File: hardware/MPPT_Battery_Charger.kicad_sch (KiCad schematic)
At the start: 78 parts, among them Q24 SI7414DN-T1-E3, Q25 SI7414DN-T1-E3, Q5 SI7414DN-T1-E3, Q6 SI7414DN-T1-E3, Q8 SI2302DDS-T1-GE3, U22 BQ24650RVAT, U26 LMV321RIYLT, U28 LMV321RIYLT, U4 INA199C1DCKR

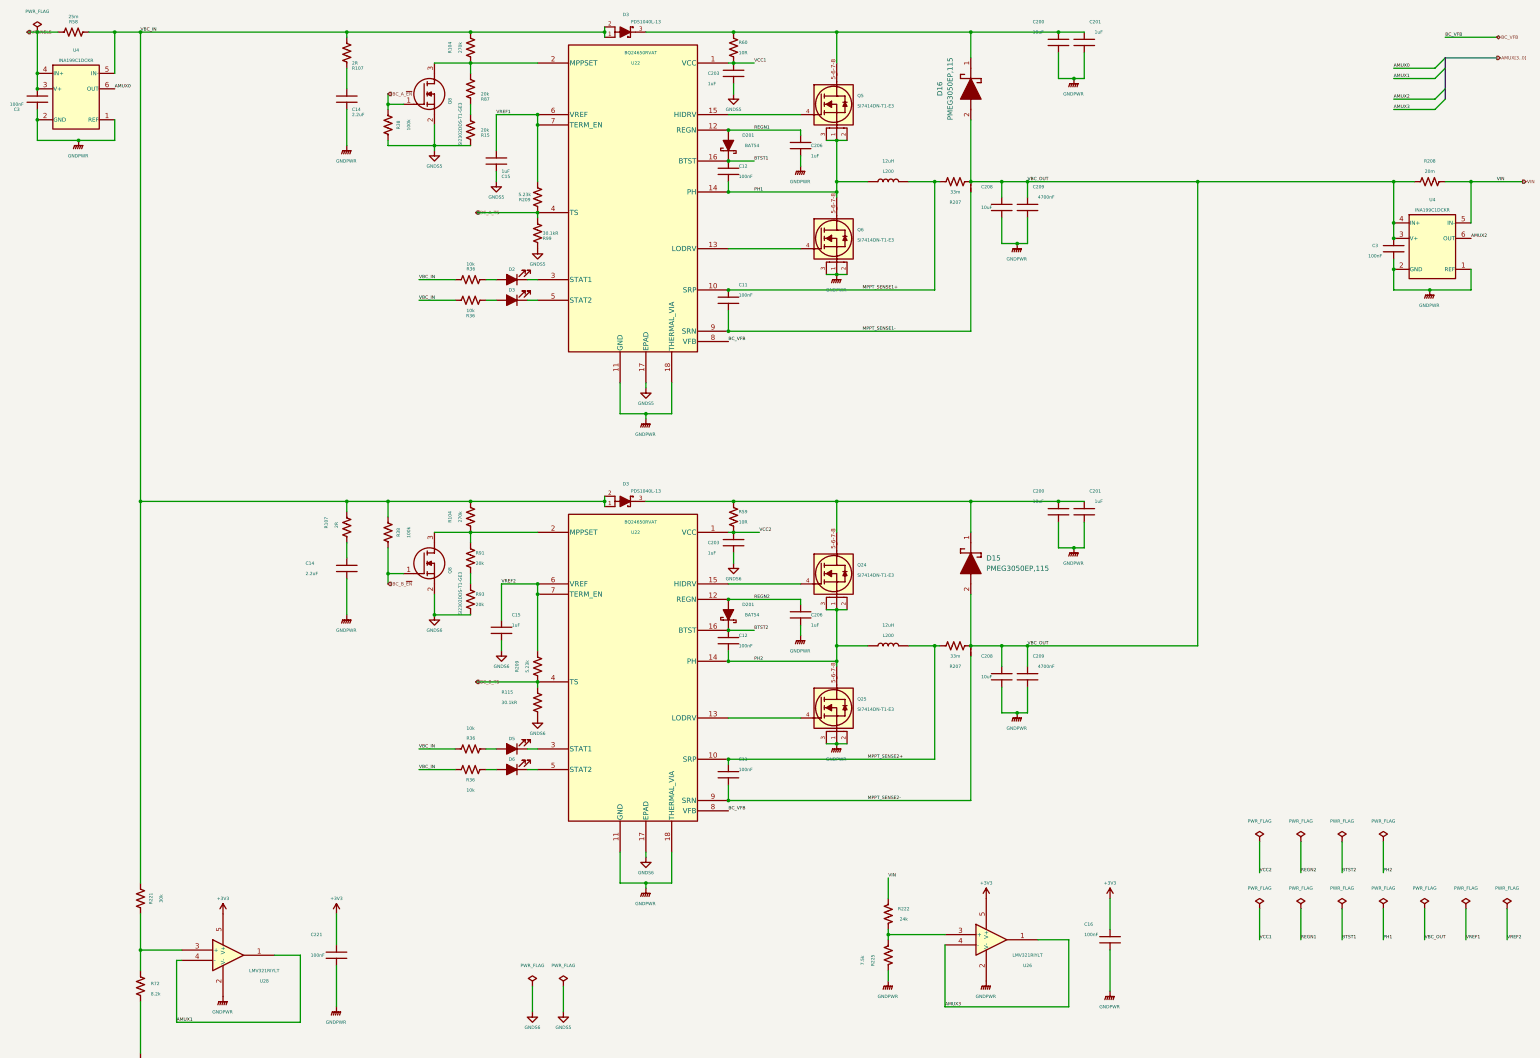
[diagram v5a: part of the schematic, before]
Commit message: hardware: Improving the readability of schematics
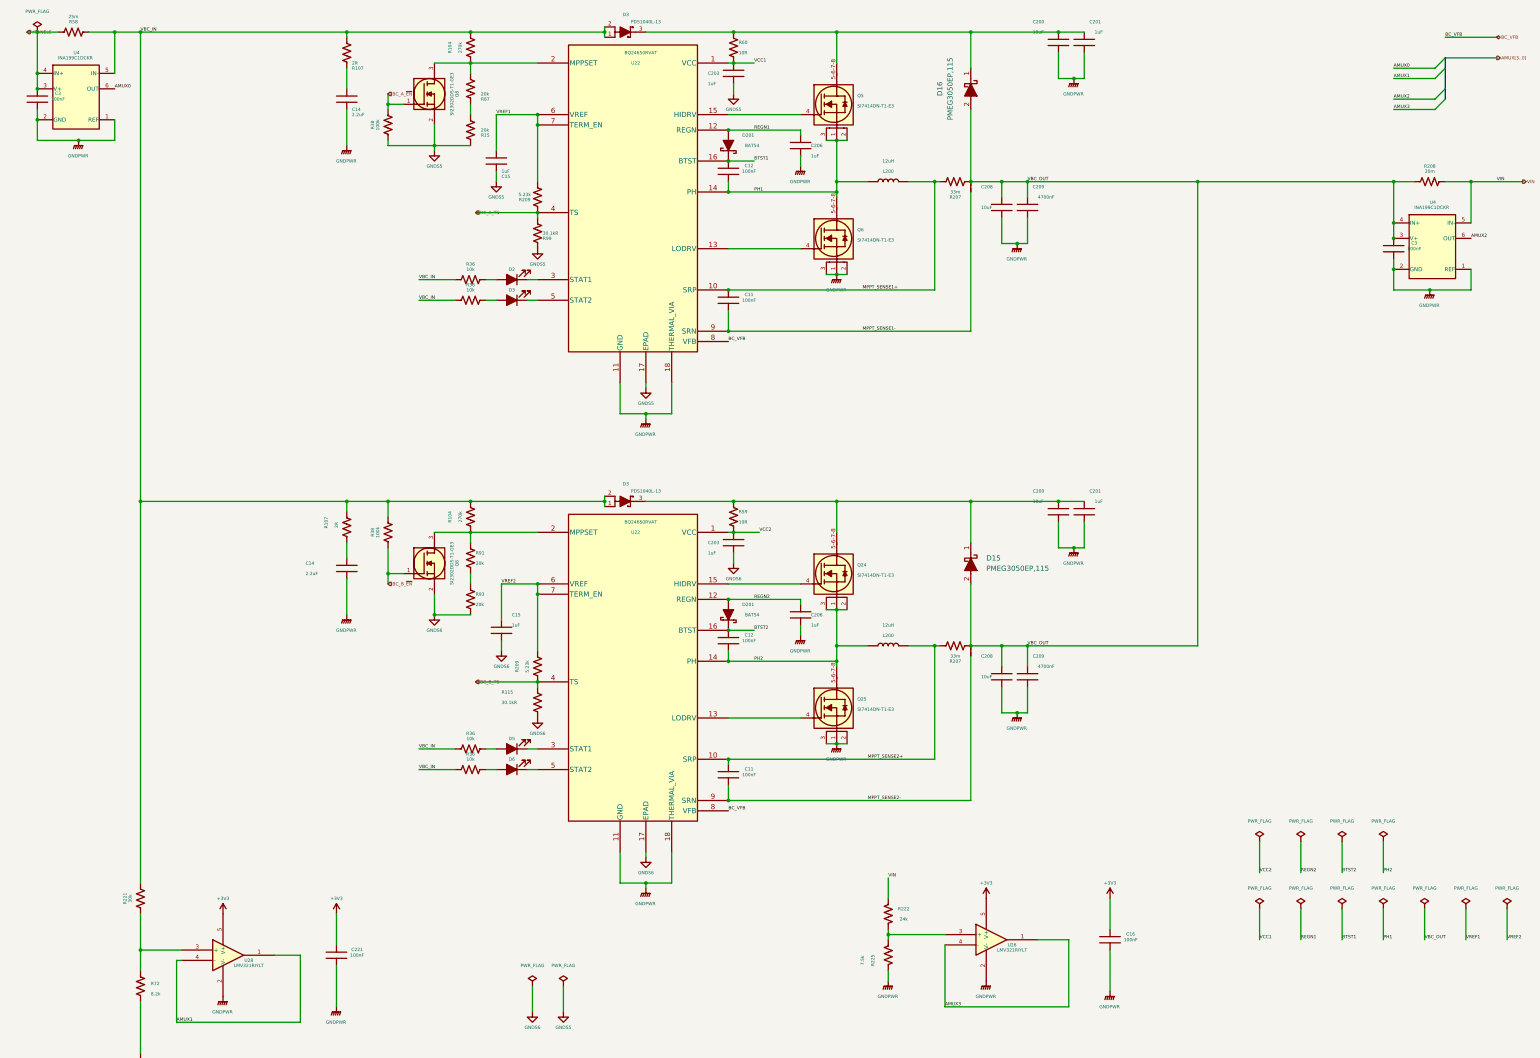
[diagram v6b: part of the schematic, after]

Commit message: hardware: Improving the readability of schematic
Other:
- note added: "ANALOG SIGNALS"
- note added: "POWER FLAGS"
- note added: "TEST POINTS"
- moved on the sheet: C16, R222, R225, U26

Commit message: hardware: Making improvements for first release
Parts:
- C11, C12, C16, C221, C3: MPN (none) -> C0603C104K5RACTU; Manufacturer (none) -> KEMET; Package (none) -> SMD 0603; automotive Yes -> (none); automotive grade Grade 1 -> (none); capacitance 0.10 μF -> (none); category Cap -> (none); device class L1 Passive Components -> (none); device class L2 Capacitors -> (none); device class L3 Ceramic Capacitors -> (none); digikey description CAP CER 0.1UF 50V X7R 0603 -> (none); digikey part number 399-5089-2-ND -> (none); height 0.87mm -> (none); lead free Yes -> (none); library id 73022d3323b2b2b8 -> (none); manufacturer KEMET -> (none); material Ceramic -> (none); mouser part number 80-C0603C104K5R7867 -> (none); package 0603 -> (none); rohs Yes -> (none); temperature characteristic X7R -> (none); temperature coefficient 30ppm/°C -> (none); temperature range high +125°C -> (none); temperature range low -55°C -> (none); tolerance 0.1 -> (none); voltage rating 50 V -> (none)
- C15, C201, C203, C206: MPN (none) -> C0805C105K5RACTU; Manufacturer (none) -> KEMET; Package (none) -> SMD 0805; capacitance 1uF -> (none); category Cap -> (none); device class L1 Passive Components -> (none); device class L2 Capacitors -> (none); device class L3 Ceramic Capacitors -> (none); digikey description CAP CER 1UF 50V X7R 0805 -> (none); digikey part number 399-7409-2-ND -> (none); height 1.4mm -> (none); ipc land pattern name CAPC200125X787 -> (none); lead free yes -> (none); library id ac83af3950e2a3c3 -> (none); manufacturer Kemet -> (none); material Ceramic -> (none); mouser description Multilayer Ceramic Capacitors MLCC - SMD/SMT 1uF 50 Volts 1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 -> (none); mouser part number 80-C0805C105K5R -> (none); package 0805 (2012 metric) -> (none); rohs yes -> (none); standoff height 0mm -> (none); temperature characteristic X7R -> (none); temperature range high +125°C -> (none); temperature range low -55°C -> (none); tolerance 10% -> (none); voltage rating 50V -> (none)
- C200, C208: MPN (none) -> C1210C106K5RACTU; Manufacturer (none) -> KEMET; Package (none) -> SMD 1210; automotive No -> (none); capacitance 10uF -> (none); category Cap -> (none); device class L1 Passive Components -> (none); device class L2 Capacitors -> (none); device class L3 Ceramic Capacitors -> (none); digikey description CAP CER 10UF 50V X7R 1210 -> (none); digikey part number 399-11629-1-ND -> (none); height 2.8mm -> (none); ipc land pattern name CAPC320250X250 -> (none); lead free Yes -> (none); library id 80b9cd679ce51e4b -> (none); manufacturer KEMET -> (none); material Ceramic -> (none); mouser description Multilayer Ceramic Capacitors MLCC - SMD/SMT 50volts 10uF 1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 -> (none); mouser part number 80-C1210C106K5R -> (none); package 1210 -> (none); rohs Yes -> (none); temperature characteristic X7R -> (none); temperature coefficient 15% -> (none); temperature range high +125°C -> (none); temperature range low -55°C -> (none); tolerance 10% -> (none); voltage rating 50V -> (none)
- JP2: value SolderJumper_2_Bridged -> N/A; MPN (none) -> N/A; Manufacturer (none) -> N/A; Package (none) -> N/A
- Q8: Height 1.12 -> (none); MPN (none) -> SI2302DDS-T1-GE3; Manufacturer (none) -> Vishay; Manufacturer_Name Vishay -> (none); Manufacturer_Part_Number SI2302DDS-T1-GE3 -> (none); Mouser Part Number 78-SI2302DDS-T1-GE3 -> (none); Mouser Price/Stock https://www.mouser.co.uk/ProductDetail/Vishay-Semiconductor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 -> (none); Package (none) -> SOT-23-3
- R207: MPN (none) -> WSL2010R0330FEA; Manufacturer (none) -> Vishay; Package (none) -> SMD 2010
- R208: Arrow Part Number WSL2010R0200FEA -> (none); Arrow Price/Stock https://www.arrow.com/en/products/wsl2010r0200fea/vishay -> (none); MPN (none) -> WSL2010R0200FEA; Manufacturer (none) -> Vishay; Manufacturer_Name Vishay -> (none); Manufacturer_Part_Number WSL2010R0200FEA -> (none); Mouser Part Number 71-WSL2010R0200FEA -> (none); Mouser Price/Stock https://www.mouser.co.uk/ProductDetail/Vishay-Dale/WSL2010R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 -> (none); Package (none) -> SMD 2010
- R221: MPN (none) -> CRCW060330K0FKEAHP; Manufacturer (none) -> Vishay; Package (none) -> SMD 0603
- R222: symbol CRCW060324K0FKEAHP:RES -> CRCW060324K0FKEAHP:CRCW060324K0FKEAHP; MPN (none) -> CRCW060324K0FKEAHP; Manufacturer (none) -> Vishay; Package (none) -> SMD 0603
- R225: MPN (none) -> CRCW06037K50FKEAHP; Manufacturer (none) -> Vishay; Package (none) -> SMD 0603; automotive Yes -> (none); automotive grade Grade 0 -> (none); category Res -> (none); composition Thick Film -> (none); device class L1 Passive Components -> (none); device class L2 Resistors -> (none); device class L3 Chip SMD Resistors -> (none); height 0.55mm -> (none); ipc land pattern name RESC16085X45 -> (none); lead free Yes -> (none); library id ac0eb7131481e5d0 -> (none); manufacturer Vishay -> (none); package 0603 -> (none); power 250mW -> (none); power rating 0.33W -> (none); resistance 7.5kΩ -> (none); rohs Yes -> (none); series CRCW-HP e3 -> (none); temperature coefficient 100ppm/°C -> (none); temperature range high +155°C -> (none); temperature range low -55°C -> (none); tolerance 1% -> (none); voltage rating 75V -> (none)
- R38: Arrow Part Number CRCW0603100KFKEAHP -> (none); Arrow Price/Stock https://www.arrow.com/en/products/crcw0603100kfkeahp/vishay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 -> (none); Height 0.55 -> (none); MPN (none) -> CRCW0603100KFKEAHP; Manufacturer (none) -> Vishay; Manufacturer_Name Vishay -> (none); Manufacturer_Part_Number CRCW0603100KFKEAHP -> (none); Mouser Part Number 71-CRCW0603100KFKEAH -> (none); Mouser Price/Stock https://www.mouser.co.uk/ProductDetail/Vishay-Dale/CRCW0603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 -> (none); Package (none) -> SMD 0603
- U22: MPN (none) -> BQ24650RVAT; Manufacturer (none) -> TI; Package (none) -> VQFN-16
- U26, U28: MPN (none) -> LMV321RIYLT; Manufacturer (none) -> STMicroelectronics; Package (none) -> SOT-23-5
- U4: symbol INA199C1DCKR:INA199xxDCK -> INA199C1DCKR:INA199C1DCKR; MPN (none) -> INA199C1DCKR; Manufacturer (none) -> TI; Package (none) -> SC70-6
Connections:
- net AMUX0: no longer U4.6 (OUT)
- net AMUX2: no longer U4.6 (OUT)
- net GNDPWR: no longer U4.1 (REF), U4.1 (REF)
- net VBC_IN: no longer U4.5 (IN-)
- net VIN: no longer U4.5 (IN-)
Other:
- moved on the sheet: U4
